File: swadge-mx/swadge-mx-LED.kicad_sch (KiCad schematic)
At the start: 13 parts

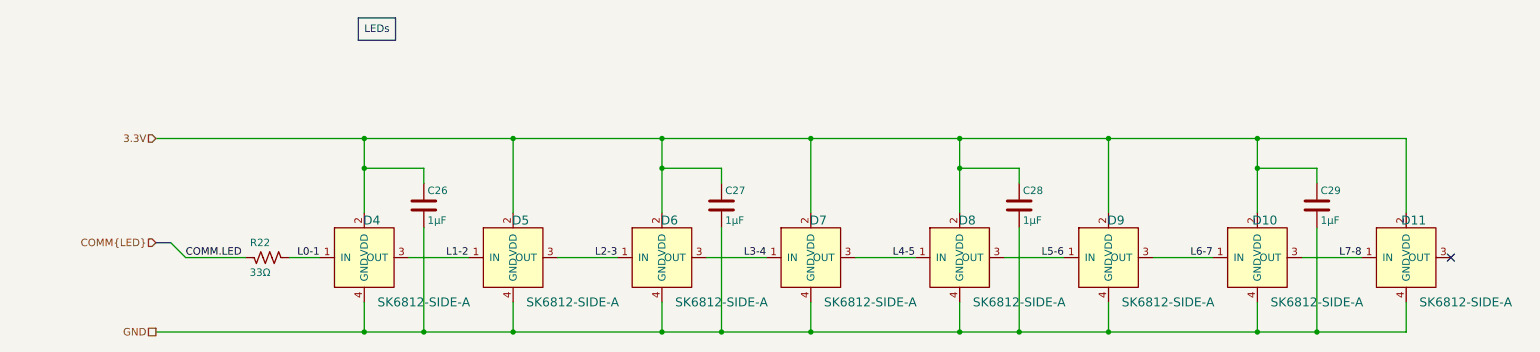
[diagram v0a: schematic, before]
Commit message: Further Subdivide Sheets
Moved all audio into one sheet, and sub-divided into DAC and amp sheets. Moved all power into one sheet and sub-divided into BMS and Buck.
Cleaned up front page a bit.
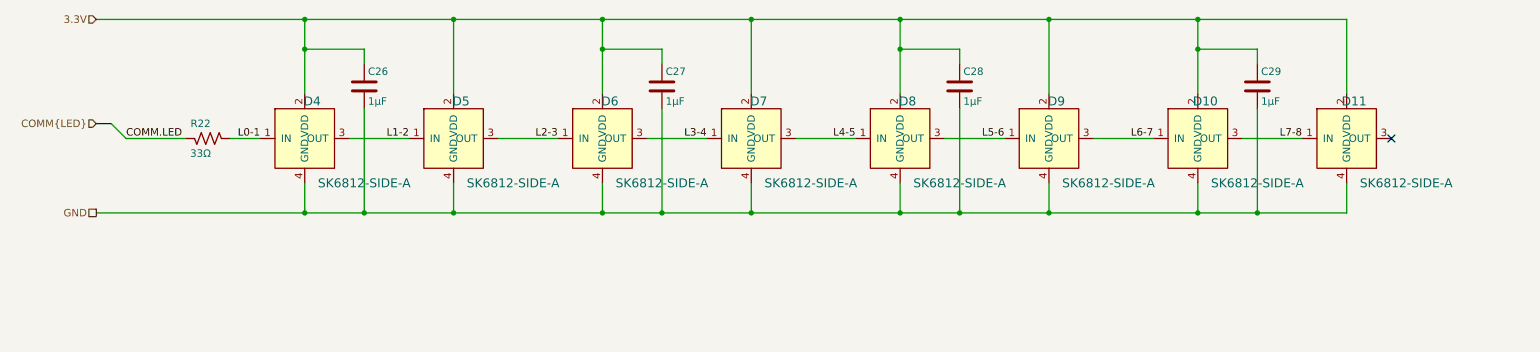
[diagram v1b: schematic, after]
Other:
- note removed: "LEDs"
- moved on the sheet: C26, C27, C28, C29, D10, D11, D4, D5, D6, D7, D8, D9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
